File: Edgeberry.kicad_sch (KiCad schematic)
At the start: 25 parts, among them P1 12Vin, Q1 BC547, Q2 BC547, Q3 BC547, SW1 SW_PUSH, U1 24LC256, U2 LM2596S-5.0

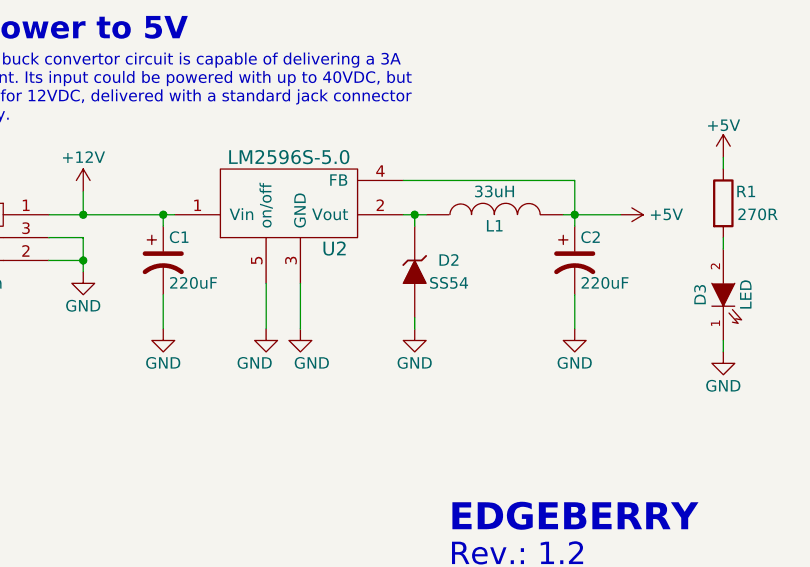
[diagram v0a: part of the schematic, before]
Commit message: Buck convertor capacitors updated to 330uF
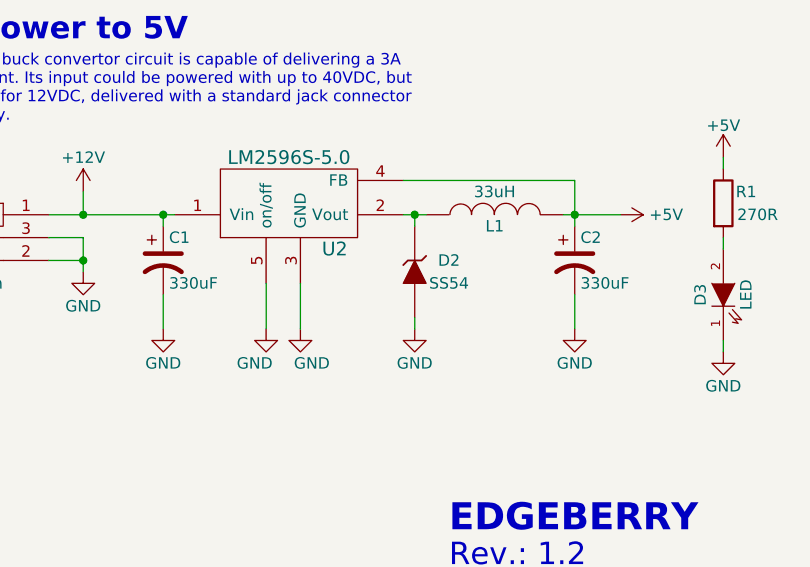
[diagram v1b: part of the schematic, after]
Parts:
- C1, C2: value 220uF -> 330uF
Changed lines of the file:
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@@
       (effects (font (size 1.27 1.27)) (justify left))
     )
-    (property "Value" "220uF" (id 1) (at 150.495 143.51 0)
+    (property "Value" "330uF" (id 1) (at 150.495 143.51 0)
       (effects (font (size 1.27 1.27)) (justify left))
     )
@@
       (effects (font (size 1.27 1.27)) (justify left))
     )
-    (property "Value" "220uF" (id 1) (at 196.215 143.51 0)
+    (property "Value" "330uF" (id 1) (at 196.215 143.51 0)
       (effects (font (size 1.27 1.27)) (justify left))
     )
@@
     )
     (path "/00000000-0000-0000-0000-00005b755152"
-      (reference "C1") (unit 1) (value "220uF") (footprint "Capacitors_SMD:c_elec_8x10")
+      (reference "C1") (unit 1) (value "330uF") (footprint "Capacitors_SMD:c_elec_8x10")
     )
     (path "/00000000-0000-0000-0000-00005b7551cf"
-      (reference "C2") (unit 1) (value "220uF") (footprint "Capacitors_SMD:c_elec_8x10")
+      (reference "C2") (unit 1) (value "330uF") (footprint "Capacitors_SMD:c_elec_8x10")
     )
     (path "/00000000-0000-0000-0000-00005c0be1df"

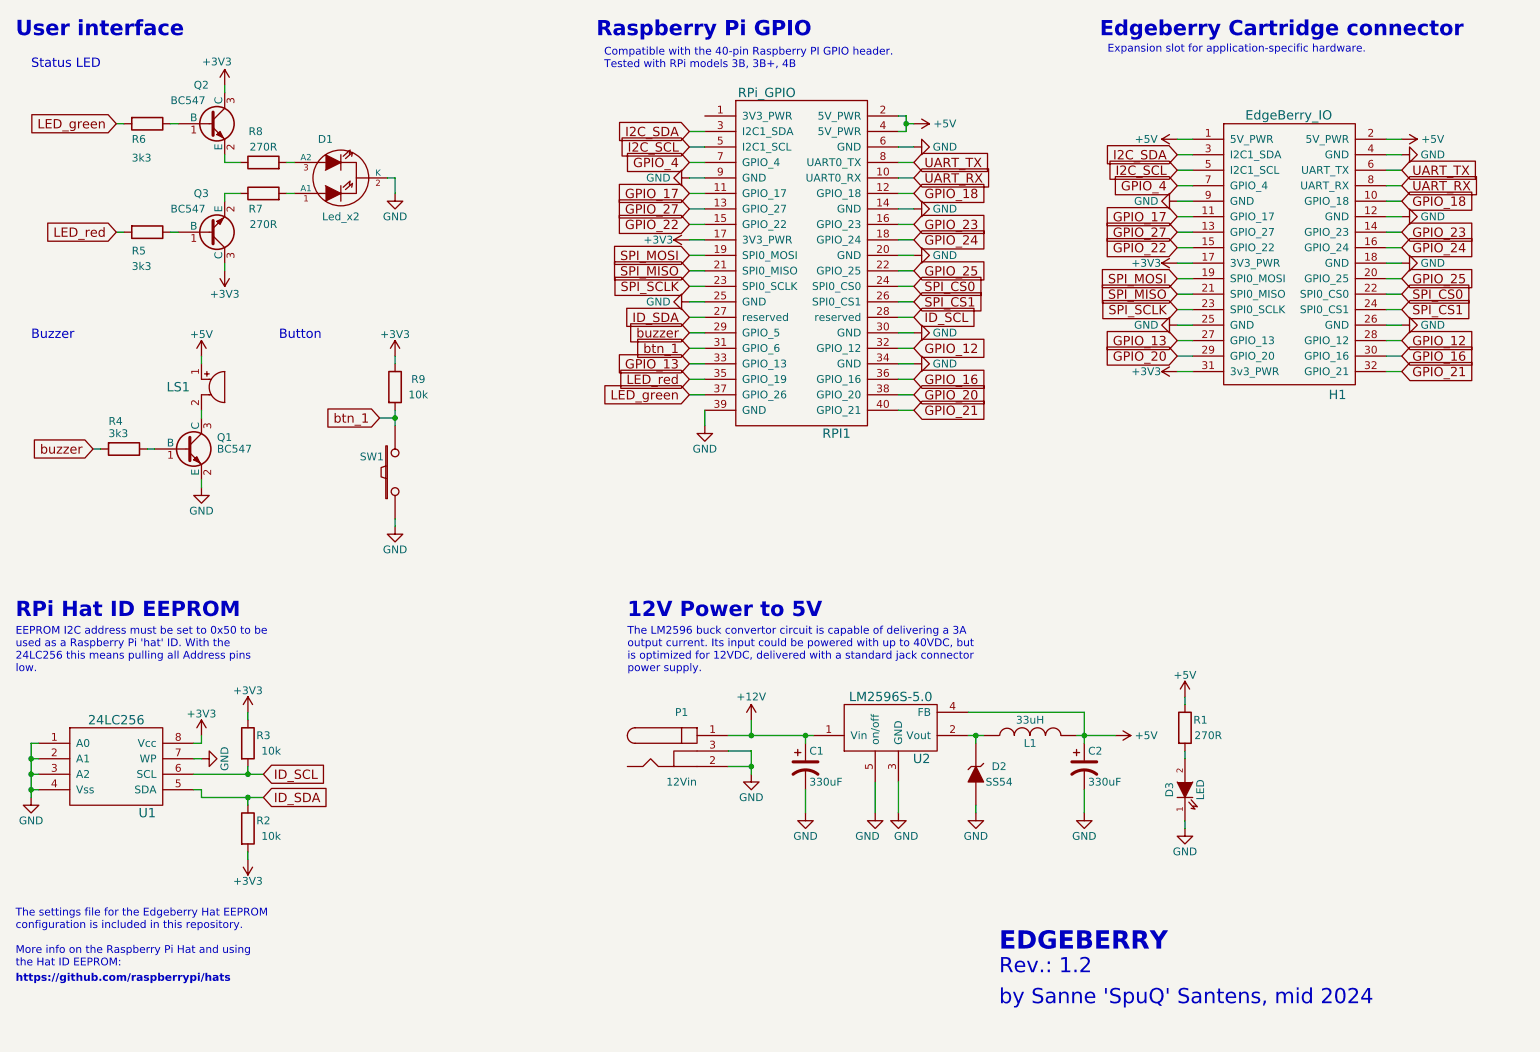
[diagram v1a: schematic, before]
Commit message: EEPROM write protection circuit + update version to 1.3
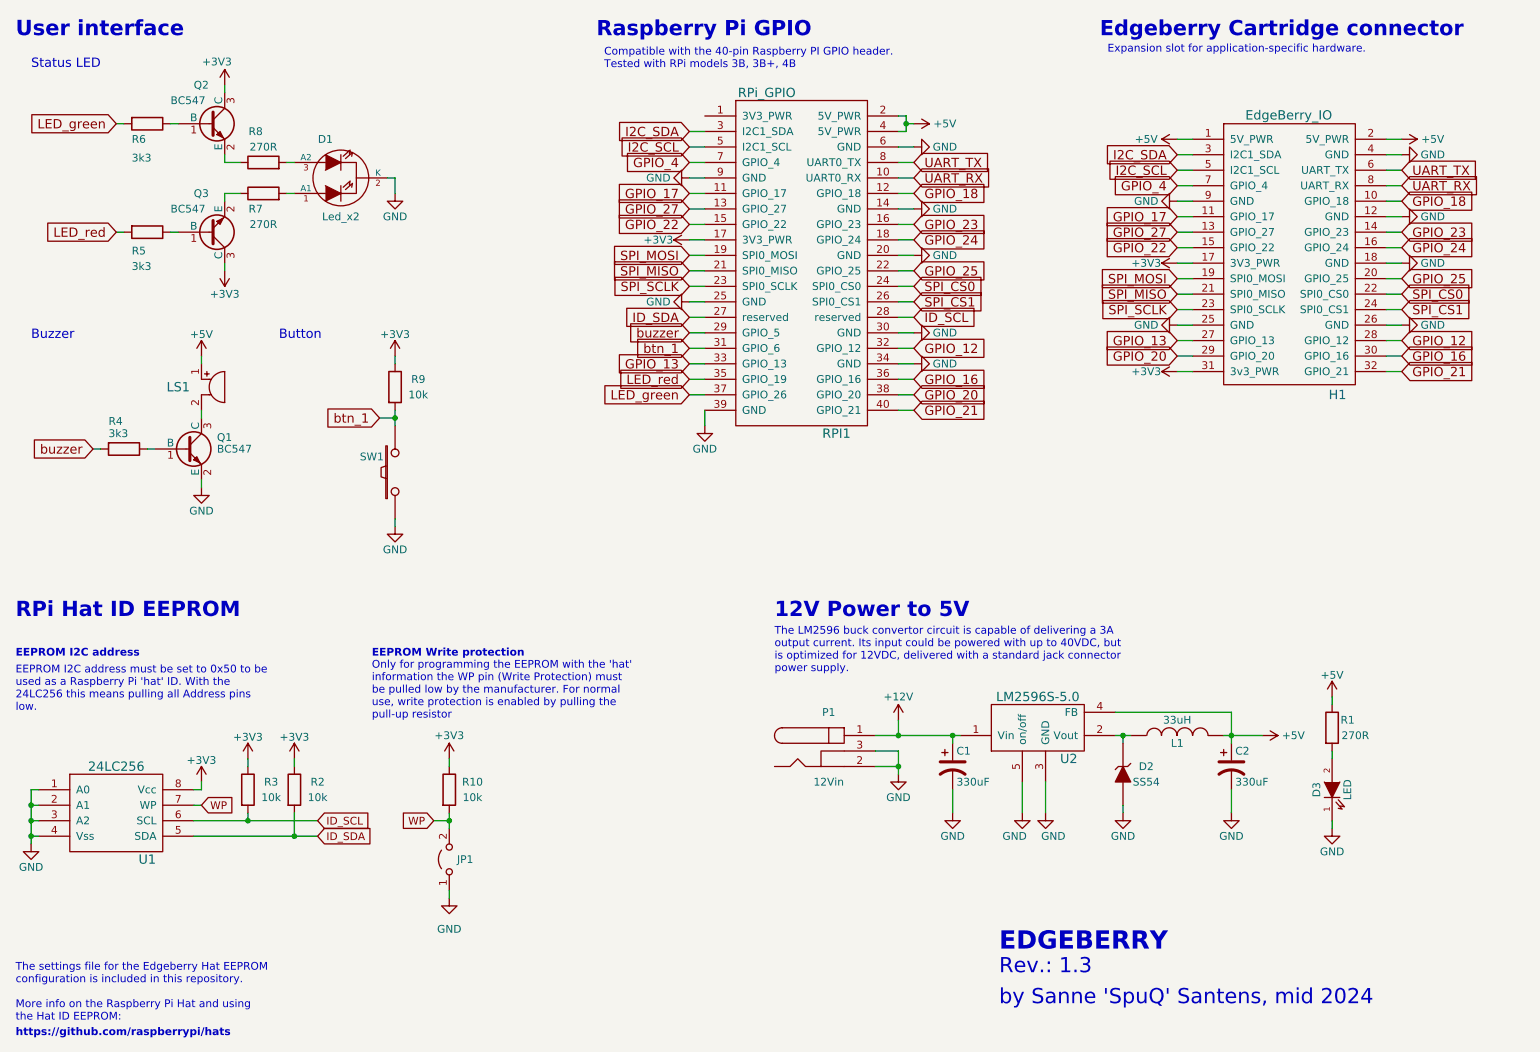
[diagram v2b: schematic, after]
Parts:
- added JP1: Jumper_2_Open, Connector_PinHeader_2.54mm:PinHeader_1x02_P2.54mm_Vertical, symbol Jumper:Jumper_2_Open
- added R10: 10k, Resistor_SMD:R_0805_2012Metric, symbol EdgeBerry-rescue:R
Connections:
- net +3V3: now also R2.1, R10.1; no longer R2.2
- net GND: now also JP1.1 (A); no longer U1.7 (WP)
- net ID_SDA: now also R2.2; no longer R2.1
- new net WP: JP1.2 (B), R10.2, U1.7 (WP)
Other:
- note added: "EEPROM I2C address"
- note added: "EEPROM Write protection"
- note added: "Only for programming the EEPROM with the 'hat' information the WP pin (Write Protection) must be pulled low by the manufacturer. For normal use, write protection is enabled by pulling the pull-up resistor"
- note added: "Rev.: 1.3"
- note removed: "Rev.: 1.2"
- moved on the sheet: C1, C2, D2, D3, L1, P1, R1, R2, R3, U1, U2

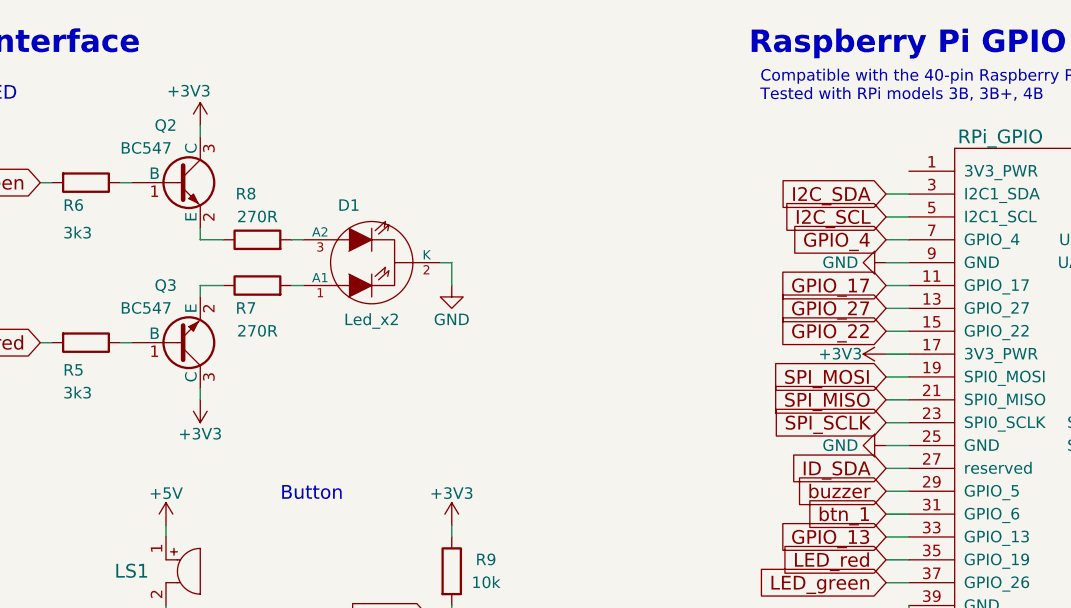
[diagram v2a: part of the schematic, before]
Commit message: Status LED on 5V instead of 3V3 + silkscreen aesthetics
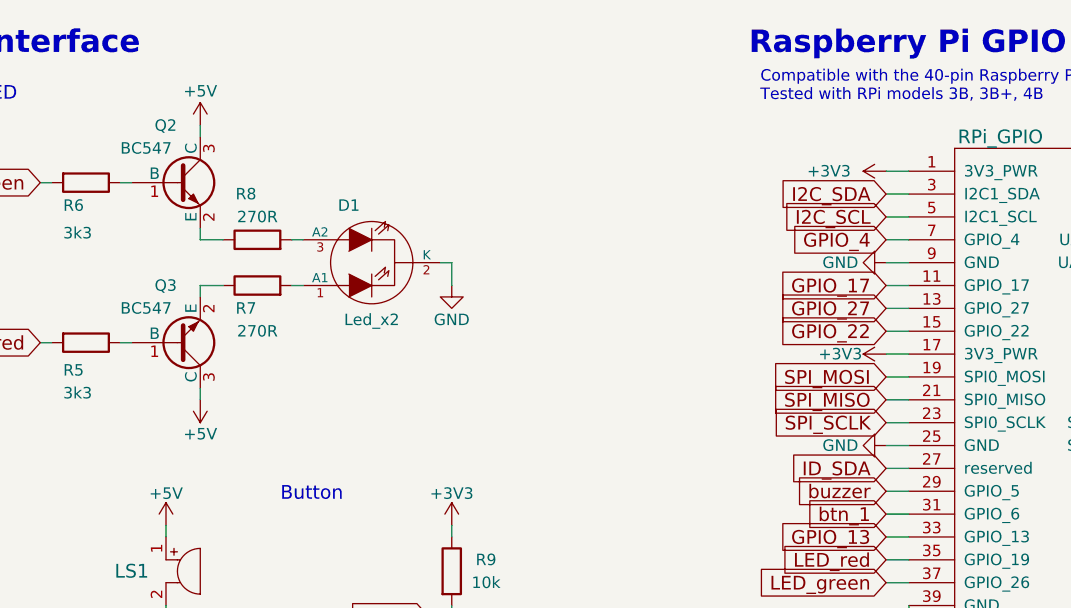
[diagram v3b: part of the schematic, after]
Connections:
- net +3V3: now also RPI1.1 (3V3_PWR); no longer Q2.3 (C), Q3.3 (C)
- net +5V: now also Q2.3 (C), Q3.3 (C)
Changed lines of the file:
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@@
+    (stroke (width 0) (type default) (color 0 0 0 0))
+  )
+  (wire (pts (xy 130.81 34.29) (xy 133.35 34.29))
     (stroke (width 0) (type default) (color 0 0 0 0))
   )
@@
     (property "Footprint" "" (id 2) (at 66.04 139.7 0))
     (property "Datasheet" "" (id 3) (at 66.04 139.7 0))
-    (pin "1")
-  )
-  (symbol (lib_id "EdgeBerry-rescue:+3V3") (at 54.61 59.69 180) (unit 1)
-    (in_bom yes) (on_board yes)
-    (property "Reference" "#PWR015" (id 0) (at 54.61 55.88 0)
-      (effects (font (size 1.27 1.27)) hide)
-    )
-    (property "Value" "+3V3" (id 1) (at 54.61 63.5 0))
-    (property "Footprint" "" (id 2) (at 54.61 59.69 0))
-    (property "Datasheet" "" (id 3) (at 54.61 59.69 0))
-    (pin "1")
-  )
-  (symbol (lib_id "EdgeBerry-rescue:+3V3") (at 54.61 29.21 0) (unit 1)
-    (in_bom yes) (on_board yes)
-    (property "Reference" "#PWR09" (id 0) (at 54.61 33.02 0)
-      (effects (font (size 1.27 1.27)) hide)
-    )
-    (property "Value" "+3V3" (id 1) (at 53.34 25.4 0))
-    (property "Footprint" "" (id 2) (at 54.61 29.21 0))
-    (property "Datasheet" "" (id 3) (at 54.61 29.21 0))
     (pin "1")
   )
@@
     (pin "2")
   )
+  (symbol (lib_id "power:+5V") (at 54.61 59.69 180) (unit 1)
+    (in_bom yes) (on_board yes)
+    (property "Reference" "#PWR0104" (id 0) (at 54.61 55.88 0)
+      (effects (font (size 1.27 1.27)) hide)
+    )
+    (property "Value" "+5V" (id 1) (at 54.61 63.5 0))
+    (property "Footprint" "" (id 2) (at 54.61 59.69 0)
+      (effects (font (size 1.27 1.27)) hide)
+    )
+    (property "Datasheet" "" (id 3) (at 54.61 59.69 0)
+      (effects (font (size 1.27 1.27)) hide)
+    )
+    (pin "1")
+  )
+  (symbol (lib_id "EdgeBerry-rescue:+3V3") (at 130.81 34.29 90) (unit 1)
+    (in_bom yes) (on_board yes)
+    (property "Reference" "#PWR?" (id 0) (at 134.62 34.29 0)
+      (effects (font (size 1.27 1.27)) hide)
+    )
+    (property "Value" "+3V3" (id 1) (at 124.46 34.29 90))
+    (property "Footprint" "" (id 2) (at 130.81 34.29 0))
+    (property "Datasheet" "" (id 3) (at 130.81 34.29 0))
+    (pin "1")
+  )
+  (symbol (lib_id "power:+5V") (at 54.61 29.21 0) (unit 1)
+    (in_bom yes) (on_board yes)
+    (property "Reference" "#PWR0103" (id 0) (at 54.61 33.02 0)
+      (effects (font (size 1.27 1.27)) hide)
+    )
+    (property "Value" "+5V" (id 1) (at 54.61 25.4 0))
+    (property "Footprint" "" (id 2) (at 54.61 29.21 0)
+      (effects (font (size 1.27 1.27)) hide)
+    )
+    (property "Datasheet" "" (id 3) (at 54.61 29.21 0)
+      (effects (font (size 1.27 1.27)) hide)
+    )
+    (pin "1")
+  )
   (symbol (lib_id "power:GND") (at 91.44 162.56 0) (unit 1)
     (in_bom yes) (on_board yes) (fields_autoplaced)
@@
       (reference "#PWR08") (unit 1) (value "GND") (footprint "")
     )
-    (path "/00000000-0000-0000-0000-00005cc8c6e8"
-      (reference "#PWR09") (unit 1) (value "+3V3") (footprint "")
-    )
     (path "/00000000-0000-0000-0000-00005c95a1f1"
       (reference "#PWR010") (unit 1) (value "+3V3") (footprint "")
@@
       (reference "#PWR014") (unit 1) (value "GND") (footprint "")
     )
-    (path "/00000000-0000-0000-0000-00005cc8c65c"
-      (reference "#PWR015") (unit 1) (value "+3V3") (footprint "")
-    )
     (path "/00000000-0000-0000-0000-00005b754b9f"
       (reference "#PWR016") (unit 1) (value "GND") (footprint "")
@@
       (reference "#PWR0102") (unit 1) (value "GND") (footprint "")
     )
+    (path "/96916265-4653-41c3-9a80-f6775aa2b630"
+      (reference "#PWR0103") (unit 1) (value "+5V") (footprint "")
+    )
+    (path "/1eae0866-fb43-460e-ba70-4206816f3ae0"
+      (reference "#PWR0104") (unit 1) (value "+5V") (footprint "")
+    )
+    (path "/59ba752a-b2a2-4535-9bd8-a06a7b8b7a31"
+      (reference "#PWR?") (unit 1) (value "+3V3") (footprint "")
+    )
     (path "/00000000-0000-0000-0000-00005b755152"
